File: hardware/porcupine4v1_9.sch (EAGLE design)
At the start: 29 parts, among them X1 PROGCON

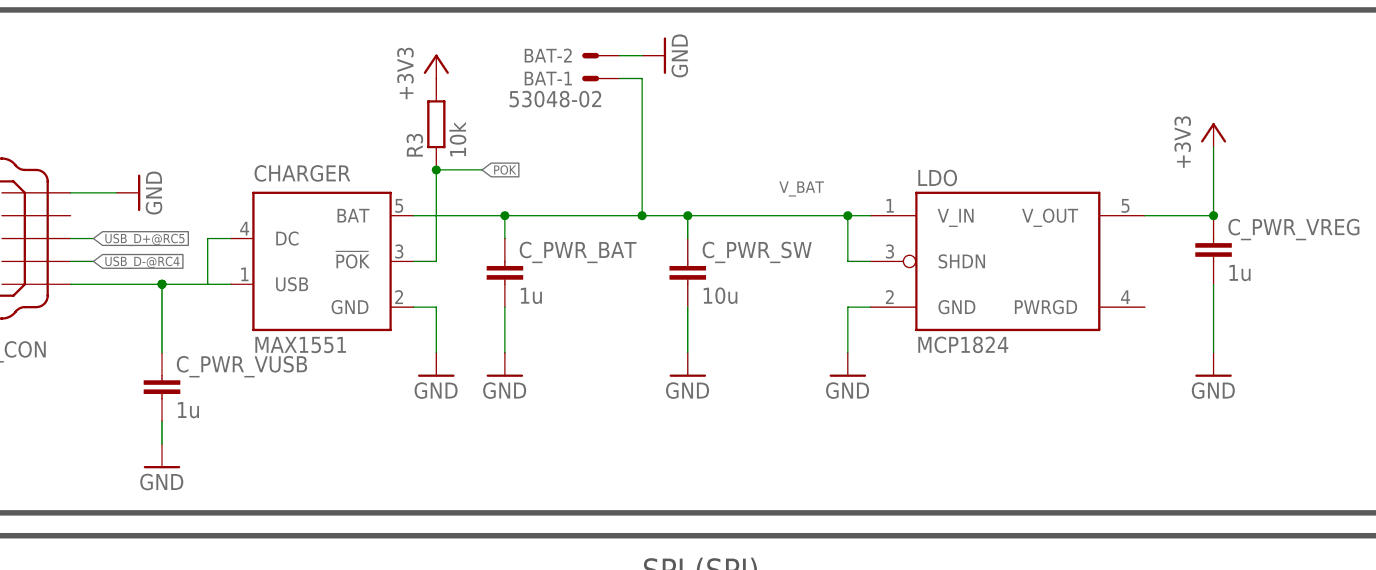
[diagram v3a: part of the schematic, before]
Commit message: hardware version 4v1_9 updated, removed c_pwr_sw capacitor
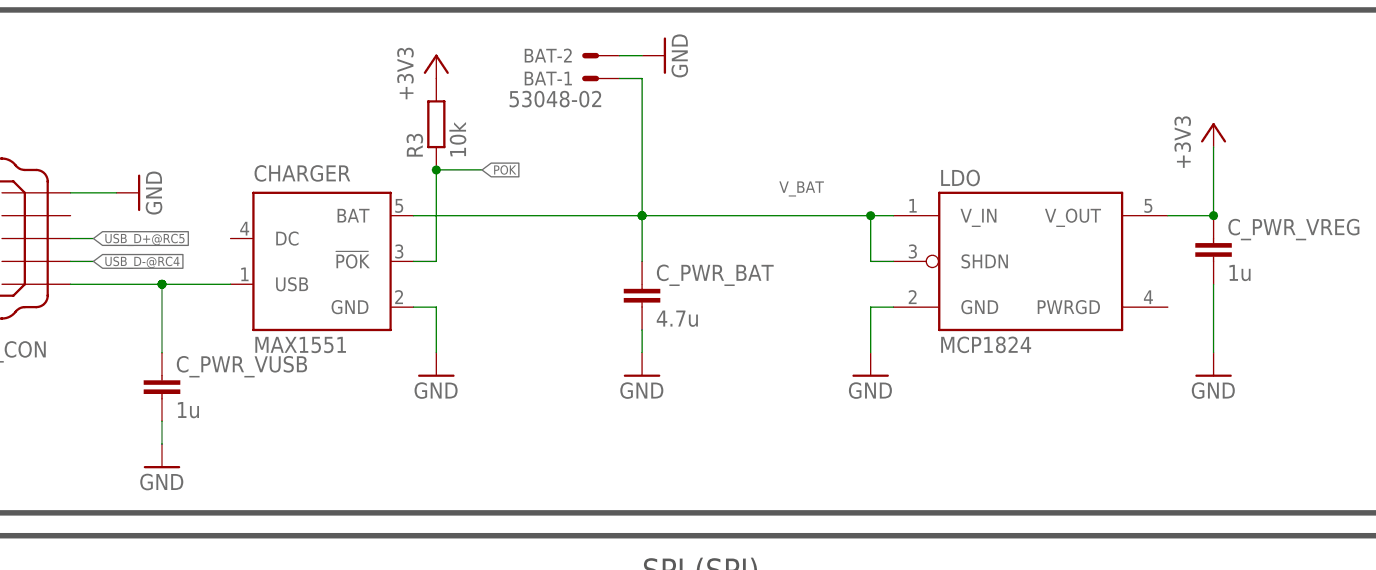
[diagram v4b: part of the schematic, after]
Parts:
- removed C_PWR_SW: 10u, rcl:C-EUC0805K
- C_PWR_BAT: value 1u -> 4.7u
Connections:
- net GND: no longer C_PWR_SW.2
- net V_BAT: no longer C_PWR_SW.1
- net V_USB: no longer CHARGER.DC
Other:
- moved on the sheet: C_PWR_BAT, LDO
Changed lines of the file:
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@@
 <?xml version="1.0" encoding="utf-8"?>
 <!DOCTYPE eagle SYSTEM "eagle.dtd">
-<eagle version="6.5.0">
+<eagle version="6.6.0">
 <drawing>
 <settings>
@@
 <part name="GND21" library="supply1" deviceset="GND" device=""/>
 <part name="GND23" library="supply1" deviceset="GND" device=""/>
-<part name="C_PWR_SW" library="rcl" deviceset="C-EU" device="C0805K" value="10u"/>
-<part name="GND24" library="supply1" deviceset="GND" device=""/>
 <part name="GND25" library="supply1" deviceset="GND" device=""/>
 <part name="+3V1" library="supply1" deviceset="+3V3" device=""/>
 <part name="CHARGER" library="maxim" deviceset="MAX1551" device=""/>
 <part name="GND27" library="supply1" deviceset="GND" device=""/>
-<part name="C_PWR_BAT" library="rcl" deviceset="C-EU" device="C0603K" value="1u"/>
+<part name="C_PWR_BAT" library="rcl" deviceset="C-EU" device="C0603K" value="4.7u"/>
 <part name="ACCELEROMETER" library="HedgehogLib" deviceset="ADXL345" device=""/>
 <part name="GND28" library="supply1" deviceset="GND" device=""/>
@@
 </part>
 <part name="GND8" library="supply1" deviceset="GND" device=""/>
-<part name="LDO" library="HedgehogLib" deviceset="MCP1824" device=""/>
 <part name="BAT" library="con-molex" deviceset="53?-02" device="048"/>
 <part name="12MHZ_RESONATOR" library="HedgehogLib" deviceset="RESONATOR" device="PRQC-C">
 <attribute name="DIGIKEY" value="http://www.digikey.de/product-detail/de/PRQC12.00CR5010X000/478-6318-1-ND/2506334"/>
 </part>
+<part name="LDO" library="HedgehogLib" deviceset="MCP1824" device=""/>
 </parts>
 <sheets>
@@
 <instance part="GND21" gate="1" x="30.48" y="71.12"/>
 <instance part="GND23" gate="1" x="86.36" y="116.84" rot="R90"/>
-<instance part="C_PWR_SW" gate="G$1" x="88.9" y="93.98"/>
-<instance part="GND24" gate="1" x="88.9" y="81.28"/>
-<instance part="GND25" gate="1" x="106.68" y="81.28"/>
+<instance part="GND25" gate="1" x="109.22" y="81.28"/>
 <instance part="+3V1" gate="G$1" x="147.32" y="109.22"/>
 <instance part="CHARGER" gate="G$1" x="48.26" y="93.98"/>
-<instance part="GND27" gate="1" x="68.58" y="81.28"/>
-<instance part="C_PWR_BAT" gate="G$1" x="68.58" y="93.98"/>
+<instance part="GND27" gate="1" x="83.82" y="81.28"/>
+<instance part="C_PWR_BAT" gate="G$1" x="83.82" y="91.44"/>
 <instance part="ACCELEROMETER" gate="ACCELEROMETER" x="119.38" y="22.86"/>
 <instance part="GND28" gate="1" x="104.14" y="7.62"/>
@@
 </instance>
 <instance part="GND8" gate="1" x="60.96" y="81.28"/>
-<instance part="LDO" gate="LDO" x="124.46" y="93.98"/>
 <instance part="BAT" gate="-1" x="78.74" y="114.3" rot="R180"/>
 <instance part="BAT" gate="-2" x="78.74" y="116.84" rot="R180"/>
@@
 <attribute name="NAME" x="259.08" y="58.42" size="1.4224" layer="95"/>
 </instance>
+<instance part="LDO" gate="LDO" x="127" y="93.98"/>
 </instances>
 <busses>
@@
 </segment>
 <segment>
-<wire x1="88.9" y1="83.82" x2="88.9" y2="88.9" width="0.1524" layer="91"/>
-<pinref part="C_PWR_SW" gate="G$1" pin="2"/>
-<pinref part="GND24" gate="1" pin="GND"/>
-</segment>
-<segment>
-<wire x1="109.22" y1="88.9" x2="106.68" y2="88.9" width="0.1524" layer="91"/>
-<wire x1="106.68" y1="88.9" x2="106.68" y2="83.82" width="0.1524" layer="91"/>
+<wire x1="111.76" y1="88.9" x2="109.22" y2="88.9" width="0.1524" layer="91"/>
+<wire x1="109.22" y1="88.9" x2="109.22" y2="83.82" width="0.1524" layer="91"/>
 <pinref part="GND25" gate="1" pin="GND"/>
 <pinref part="LDO" gate="LDO" pin="GND"/>
@@
 </segment>
 <segment>
-<wire x1="68.58" y1="83.82" x2="68.58" y2="88.9" width="0.1524" layer="91"/>
+<wire x1="83.82" y1="83.82" x2="83.82" y2="86.36" width="0.1524" layer="91"/>
 <pinref part="GND27" gate="1" pin="GND"/>
 <pinref part="C_PWR_BAT" gate="G$1" pin="2"/>
@@
 <segment>
 <wire x1="30.48" y1="83.82" x2="30.48" y2="91.44" width="0.1524" layer="91"/>
-<wire x1="38.1" y1="91.44" x2="35.56" y2="91.44" width="0.1524" layer="91"/>
-<wire x1="35.56" y1="91.44" x2="30.48" y2="91.44" width="0.1524" layer="91"/>
+<wire x1="38.1" y1="91.44" x2="30.48" y2="91.44" width="0.1524" layer="91"/>
 <wire x1="20.32" y1="91.44" x2="30.48" y2="91.44" width="0.1524" layer="91"/>
 <junction x="30.48" y="91.44"/>
@@
 <pinref part="CHARGER" gate="G$1" pin="USB"/>
 <pinref part="USB_CON" gate="G$1" pin="1"/>
-<wire x1="35.56" y1="91.44" x2="35.56" y2="96.52" width="0.1524" layer="91"/>
-<pinref part="CHARGER" gate="G$1" pin="DC"/>
-<wire x1="35.56" y1="96.52" x2="38.1" y2="96.52" width="0.1524" layer="91"/>
 </segment>
 </net>
@@
 <pinref part="+3V1" gate="G$1" pin="+3V3"/>
 <pinref part="C_PWR_VREG" gate="G$1" pin="1"/>
-<wire x1="139.7" y1="99.06" x2="147.32" y2="99.06" width="0.1524" layer="91"/>
+<wire x1="142.24" y1="99.06" x2="147.32" y2="99.06" width="0.1524" layer="91"/>
 <wire x1="147.32" y1="106.68" x2="147.32" y2="99.06" width="0.1524" layer="91"/>
 <pinref part="LDO" gate="LDO" pin="V_OUT"/>
@@
 <net name="V_BAT" class="0">
 <segment>
-<wire x1="109.22" y1="93.98" x2="106.68" y2="93.98" width="0.1524" layer="91"/>
-<wire x1="106.68" y1="93.98" x2="106.68" y2="99.06" width="0.1524" layer="91"/>
-<wire x1="106.68" y1="99.06" x2="109.22" y2="99.06" width="0.1524" layer="91"/>
-<wire x1="106.68" y1="99.06" x2="88.9" y2="99.06" width="0.1524" layer="91"/>
-<wire x1="88.9" y1="96.52" x2="88.9" y2="99.06" width="0.1524" layer="91"/>
+<wire x1="111.76" y1="99.06" x2="109.22" y2="99.06" width="0.1524" layer="91"/>
+<wire x1="109.22" y1="99.06" x2="83.82" y2="99.06" width="0.1524" layer="91"/>
 <wire x1="81.28" y1="114.3" x2="83.82" y2="114.3" width="0.1524" layer="91"/>
 <wire x1="83.82" y1="114.3" x2="83.82" y2="99.06" width="0.1524" layer="91"/>
-<wire x1="83.82" y1="99.06" x2="88.9" y2="99.06" width="0.1524" layer="91"/>
-<wire x1="58.42" y1="99.06" x2="68.58" y2="99.06" width="0.1524" layer="91"/>
-<wire x1="68.58" y1="96.52" x2="68.58" y2="99.06" width="0.1524" layer="91"/>
-<wire x1="68.58" y1="99.06" x2="83.82" y2="99.06" width="0.1524" layer="91"/>
-<junction x="106.68" y="99.06"/>
-<junction x="88.9" y="99.06"/>
+<wire x1="58.42" y1="99.06" x2="83.82" y2="99.06" width="0.1524" layer="91"/>
+<wire x1="83.82" y1="93.98" x2="83.82" y2="99.06" width="0.1524" layer="91"/>
 <junction x="83.82" y="99.06"/>
 <label x="99.06" y="101.6" size="1.27" layer="95"/>
-<pinref part="C_PWR_SW" gate="G$1" pin="1"/>
 <pinref part="C_PWR_BAT" gate="G$1" pin="1"/>
 <pinref part="CHARGER" gate="G$1" pin="BAT"/>
-<junction x="68.58" y="99.06"/>
+<junction x="83.82" y="99.06"/>
+<pinref part="BAT" gate="-1" pin="S"/>
+<pinref part="LDO" gate="LDO" pin="V_IN"/>
 <pinref part="LDO" gate="LDO" pin="SHDN"/>
-<pinref part="LDO" gate="LDO" pin="V_IN"/>
-<pinref part="BAT" gate="-1" pin="S"/>
-</segment>
-</net>
+<wire x1="111.76" y1="93.98" x2="109.22" y2="93.98" width="0.1524" layer="91"/>
+<wire x1="109.22" y1="93.98" x2="109.22" y2="99.06" width="0.1524" layer="91"/>
+<junction x="109.22" y="99.06"/>
+</segment>
+</net>

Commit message: v4.1.9: added farnell order numbers
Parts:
- 12MHZ_RESONATOR: DIGIKEY http://www.digikey.de/product-detail/de/PRQC12.00CR5010X000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 -> (none); OC_DIGIKEY (none) -> 478-6318-1-ND
- 32KHZ_CRYSTAL: FARNELL 2101349 -> (none); OC_FARNELL (none) -> 2101349
- ACCELEROMETER: OC_FARNELL (none) -> 1853935
- LDO: OC_FARNELL (none) -> 1578387
- LIGHTSENSE: OC_FARNELL (none) -> 1182346
- PIC_CONTROLLER: OC_FARNELL (none) -> 1706311
- SDCARD_CON: OC_FARNELL (none) -> 1686452
- USB_CON: OC_FARNELL (none) -> 2112367
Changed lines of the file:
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@@
 <parts>
 <part name="GND3" library="supply1" deviceset="GND" device=""/>
-<part name="SDCARD_CON" library="HedgehogLib" deviceset="MICROSD_CONN" device=""/>
+<part name="SDCARD_CON" library="HedgehogLib" deviceset="MICROSD_CONN" device="">
+<attribute name="OC_FARNELL" value="1686452"/>
+</part>
 <part name="GND16" library="supply1" deviceset="GND" device=""/>
-<part name="LIGHTSENSE" library="HedgehogLib" deviceset="TSL250" device=""/>
-<part name="USB_CON" library="HedgehogLib" deviceset="USBCON" device=""/>
+<part name="LIGHTSENSE" library="HedgehogLib" deviceset="TSL250" device="">
+<attribute name="OC_FARNELL" value="1182346"/>
+</part>
+<part name="USB_CON" library="HedgehogLib" deviceset="USBCON" device="">
+<attribute name="OC_FARNELL" value="2112367"/>
+</part>
 <part name="GND20" library="supply1" deviceset="GND" device=""/>
 <part name="C_PWR_VUSB" library="rcl" deviceset="C-EU" device="C0603K" value="1u"/>
@@
 <part name="GND27" library="supply1" deviceset="GND" device=""/>
 <part name="C_PWR_BAT" library="rcl" deviceset="C-EU" device="C0603K" value="4.7u"/>
-<part name="ACCELEROMETER" library="HedgehogLib" deviceset="ADXL345" device=""/>
+<part name="ACCELEROMETER" library="HedgehogLib" deviceset="ADXL345" device="">
+<attribute name="OC_FARNELL" value="1853935"/>
+</part>
 <part name="GND28" library="supply1" deviceset="GND" device=""/>
 <part name="+3V3" library="supply1" deviceset="+3V3" device=""/>
@@
 <part name="C_PWR_VREG" library="rcl" deviceset="C-EU" device="C0603K" value="1u"/>
 <part name="GND31" library="supply1" deviceset="GND" device=""/>
-<part name="PIC_CONTROLLER" library="HedgehogLib" deviceset="PIC_P2V6" device=""/>
+<part name="PIC_CONTROLLER" library="HedgehogLib" deviceset="PIC_P2V6" device="">
+<attribute name="OC_FARNELL" value="1706311"/>
+</part>
 <part name="C2_32KHZ" library="rcl" deviceset="C-EU" device="C0603K" value="22p"/>
 <part name="C1_32KHZ" library="rcl" deviceset="C-EU" device="C0603K" value="22p"/>
@@
 <part name="GND1" library="supply1" deviceset="GND" device=""/>
 <part name="32KHZ_CRYSTAL" library="HedgehogLib" deviceset="SMD_CRYSTAL" device="">
-<attribute name="FARNELL" value="2101349"/>
+<attribute name="OC_FARNELL" value="2101349"/>
 </part>
 <part name="GND8" library="supply1" deviceset="GND" device=""/>
 <part name="BAT" library="con-molex" deviceset="53?-02" device="048"/>
 <part name="12MHZ_RESONATOR" library="HedgehogLib" deviceset="RESONATOR" device="PRQC-C">
-<attribute name="DIGIKEY" value="http://www.digikey.de/product-detail/de/PRQC12.00CR5010X000/478-6318-1-ND/2506334"/>
-</part>
-<part name="LDO" library="HedgehogLib" deviceset="MCP1824" device=""/>
+<attribute name="OC_DIGIKEY" value="478-6318-1-ND"/>
+</part>
+<part name="LDO" library="HedgehogLib" deviceset="MCP1824" device="">
+<attribute name="OC_FARNELL" value="1578387"/>
+</part>
 </parts>
 <sheets>
@@
 <instances>
 <instance part="GND3" gate="1" x="12.7" y="139.7"/>
-<instance part="SDCARD_CON" gate="G$1" x="17.78" y="22.86" rot="R90"/>
+<instance part="SDCARD_CON" gate="G$1" x="17.78" y="22.86" rot="R90">
+<attribute name="OC_FARNELL" x="17.78" y="22.86" size="1.778" layer="96" rot="R90" display="off"/>
+</instance>
 <instance part="GND16" gate="1" x="38.1" y="20.32" rot="R90"/>
 <instance part="LIGHTSENSE" gate="G$1" x="83.82" y="144.78" smashed="yes">
 <attribute name="VALUE" x="89.916" y="148.336" size="1.778" layer="96" rot="R270"/>
-</instance>
-<instance part="USB_CON" gate="G$1" x="15.24" y="96.52" rot="R180"/>
+<attribute name="OC_FARNELL" x="83.82" y="144.78" size="1.778" layer="96" display="off"/>
+</instance>
+<instance part="USB_CON" gate="G$1" x="15.24" y="96.52" rot="R180">
+<attribute name="OC_FARNELL" x="15.24" y="96.52" size="1.778" layer="96" rot="R180" display="off"/>
+</instance>
 <instance part="GND20" gate="1" x="27.94" y="101.6" rot="R90"/>
 <instance part="C_PWR_VUSB" gate="G$1" x="30.48" y="81.28"/>
@@
 <instance part="GND27" gate="1" x="83.82" y="81.28"/>
 <instance part="C_PWR_BAT" gate="G$1" x="83.82" y="91.44"/>
-<instance part="ACCELEROMETER" gate="ACCELEROMETER" x="119.38" y="22.86"/>
+<instance part="ACCELEROMETER" gate="ACCELEROMETER" x="119.38" y="22.86">
+<attribute name="OC_FARNELL" x="119.38" y="22.86" size="1.778" layer="96" display="off"/>
+</instance>
 <instance part="GND28" gate="1" x="104.14" y="7.62"/>
 <instance part="+3V3" gate="G$1" x="78.74" y="40.64"/>
@@
 <instance part="C_PWR_VREG" gate="G$1" x="147.32" y="96.52"/>
 <instance part="GND31" gate="1" x="147.32" y="81.28"/>
-<instance part="PIC_CONTROLLER" gate="G$1" x="213.36" y="58.42"/>
+<instance part="PIC_CONTROLLER" gate="G$1" x="213.36" y="58.42">
+<attribute name="OC_FARNELL" x="213.36" y="58.42" size="1.778" layer="96" display="off"/>
+</instance>
 <instance part="C2_32KHZ" gate="G$1" x="205.74" y="109.22" smashed="yes">
 <attribute name="NAME" x="207.264" y="109.601" size="1.778" layer="95"/>
@@
 <instance part="32KHZ_CRYSTAL" gate="G$1" x="195.58" y="111.76" smashed="yes">
 <attribute name="VALUE" x="191.262" y="114.808" size="1.4224" layer="96"/>
-<attribute name="FARNELL" x="195.58" y="111.76" size="1.778" layer="96" display="off"/>
+<attribute name="OC_FARNELL" x="195.58" y="111.76" size="1.778" layer="96" display="off"/>
 </instance>
 <instance part="GND8" gate="1" x="60.96" y="81.28"/>
@@
 <instance part="BAT" gate="-2" x="78.74" y="116.84" rot="R180"/>
 <instance part="12MHZ_RESONATOR" gate="RESONATOR" x="259.08" y="53.34" smashed="yes" rot="R180">
-<attribute name="DIGIKEY" x="259.08" y="53.34" size="1.778" layer="96" rot="R180" display="off"/>
+<attribute name="OC_DIGIKEY" x="259.08" y="53.34" size="1.778" layer="96" rot="R180" display="off"/>
 <attribute name="NAME" x="259.08" y="58.42" size="1.4224" layer="95"/>
 </instance>
-<instance part="LDO" gate="LDO" x="127" y="93.98"/>
+<instance part="LDO" gate="LDO" x="127" y="93.98">
+<attribute name="OC_FARNELL" x="127" y="93.98" size="1.778" layer="96" display="off"/>
+</instance>
 </instances>
 <busses>
